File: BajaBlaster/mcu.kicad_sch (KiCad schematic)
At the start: 4 parts, among them U1 ESP32-WROOM-32

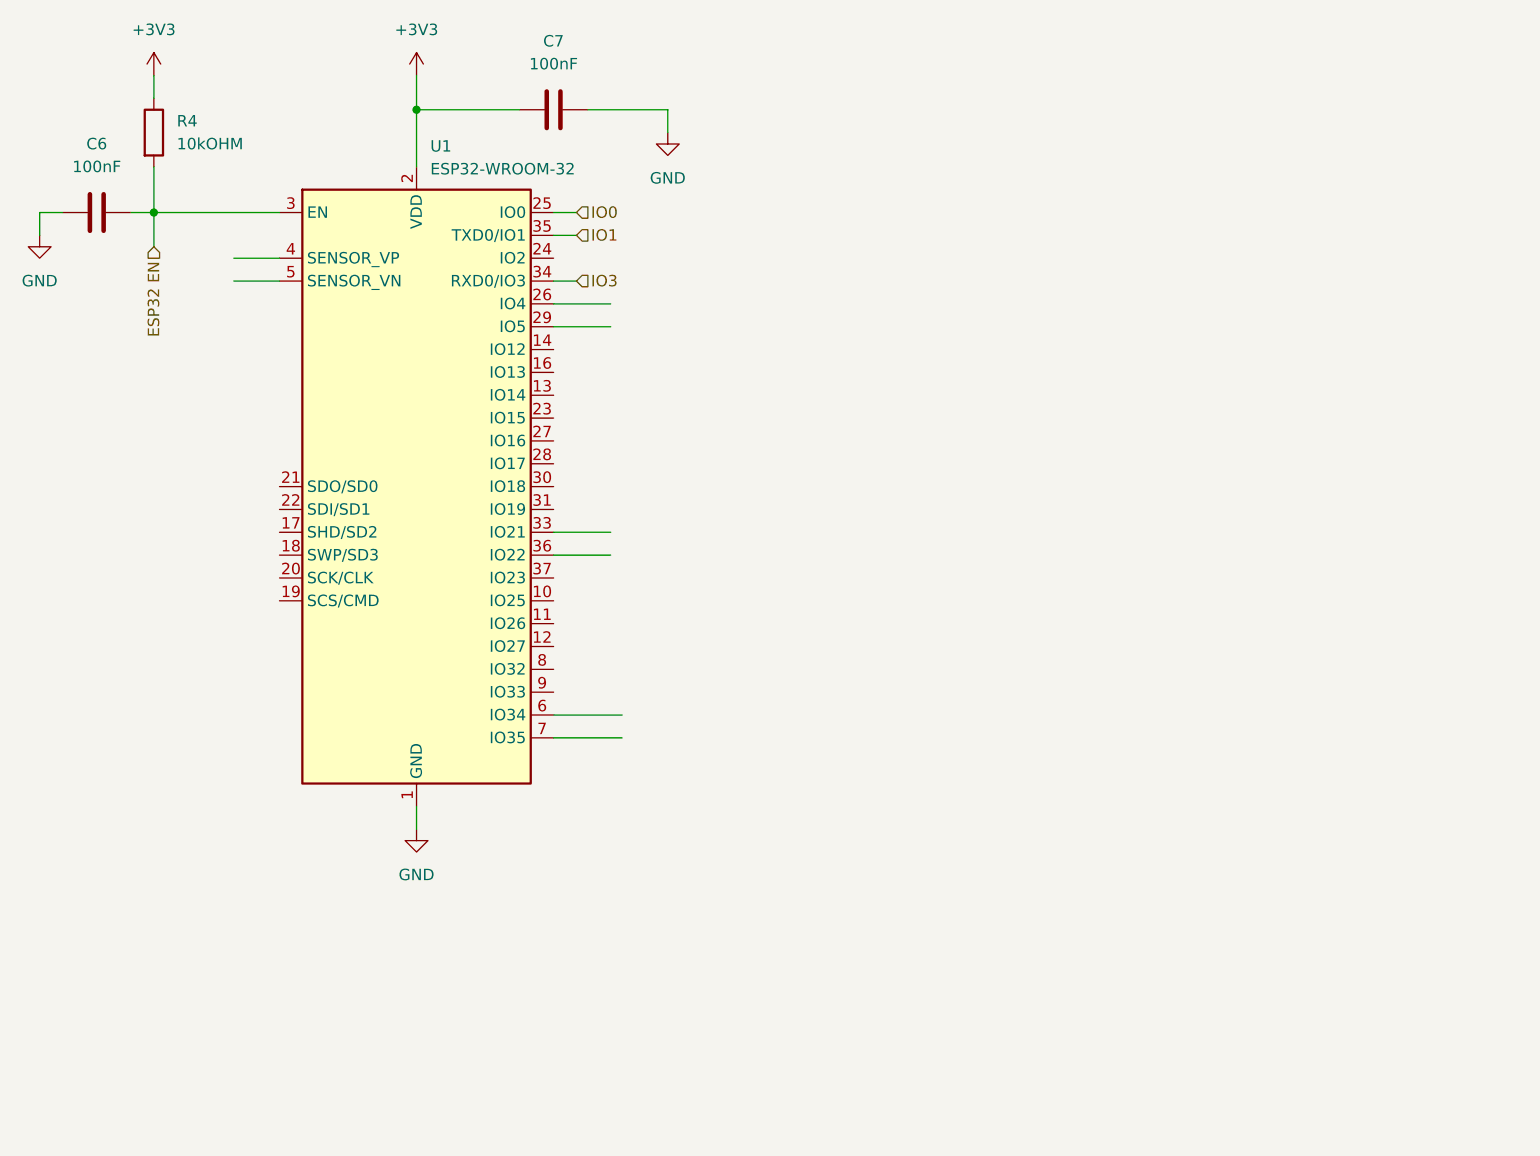
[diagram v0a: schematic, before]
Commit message: Updated mcu with wiring for MPU6050
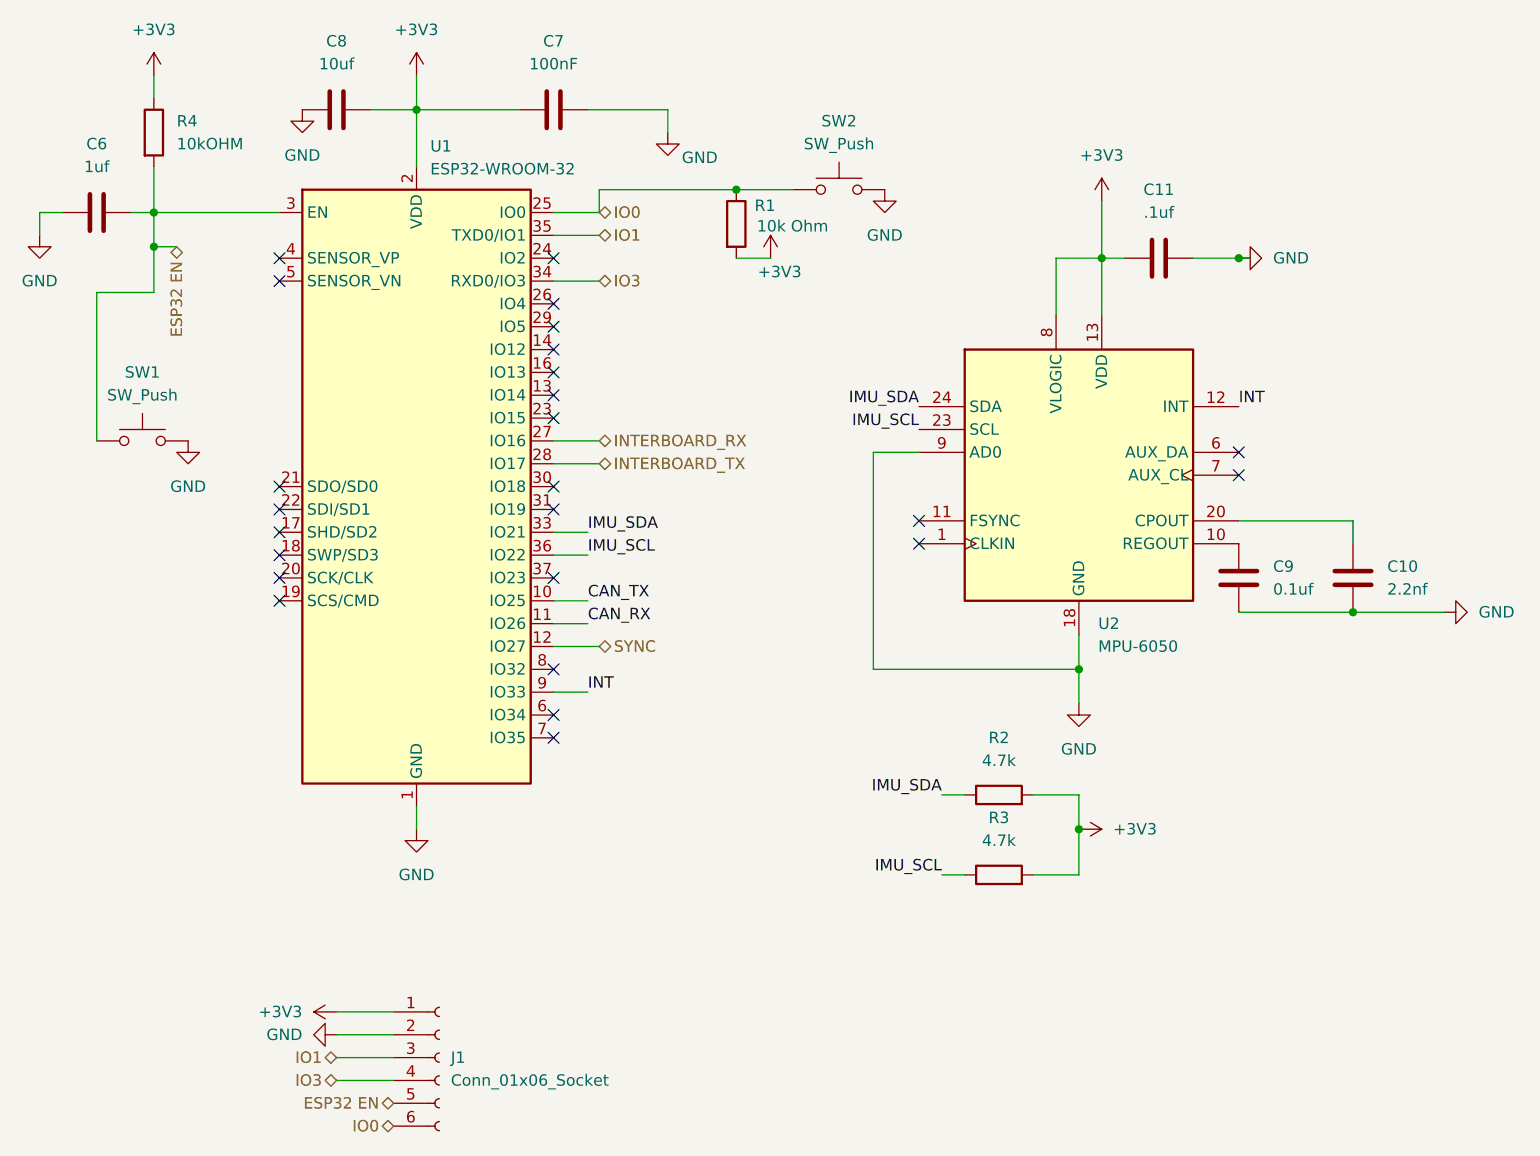
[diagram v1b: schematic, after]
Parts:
- added C10: 2.2nf, Package_SO:SOIC-8_3.9x4.9mm_P1.27mm, symbol Device:C
- added C11: .1uf, Package_SO:SOIC-8_3.9x4.9mm_P1.27mm, symbol Device:C
- added C8: 10uf, Package_SO:SOIC-8_3.9x4.9mm_P1.27mm, symbol Device:C
- added C9: 0.1uf, Package_SO:SOIC-8_3.9x4.9mm_P1.27mm, symbol Device:C
- added J1: Conn_01x06_Socket, Connector:Tag-Connect_TC2030-IDC-FP_2x03_P1.27mm_Vertical, symbol Connector:Conn_01x06_Socket
- added R1: 10k Ohm, Package_DIP:DIP-8_W7.62mm, symbol Device:R
- added R2, R3: 4.7k, Package_DIP:DIP-8_W7.62mm, symbol Device:R
- added SW1: SW_Push, Package_DIP:DIP-24_W7.62mm, symbol Switch:SW_Push
- added SW2: SW_Push, symbol Switch:SW_Push
- added U2: MPU-6050, Sensor_Motion:InvenSense_QFN-24_4x4mm_P0.5mm, symbol Sensor_Motion:MPU-6050
- C6: value 100nF -> 1uf
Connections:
- net +3V3: now also C11.1, C8.2, J1.1 (Pin_1), R1.2, R2.2, R3.2, U2.13 (VDD), U2.8 (VLOGIC)
- net ESP32 EN: now also J1.5 (Pin_5), SW1.1
- net GND: now also C10.1, C11.2, C8.1, C9.1, J1.2 (Pin_2), SW1.2, SW2.2, U2.18 (GND), U2.9 (AD0)
- net IO0: now also J1.6 (Pin_6), R1.1, SW2.1
- net IO1: now also J1.3 (Pin_3)
- net IO3: now also J1.4 (Pin_4)
- net CAN_TX: now reaches U1.10 (IO25)
- net CAN_RX: now reaches U1.11 (IO26)
- net SYNC: now reaches U1.12 (IO27)
- net INTERBOARD_RX: now reaches U1.27 (IO16)
- net INTERBOARD_TX: now reaches U1.28 (IO17)
- net IMU_SDA: now reaches U1.33 (IO21)
- net IMU_SDA: now also R2.1, U2.24 (SDA)
- net IMU_SCL: now reaches U1.36 (IO22)
- net IMU_SCL: now also R3.1, U2.23 (SCL)
- net INT: now reaches U1.9 (IO33)
- net INT: now also U2.12 (INT)
- new net: C9.2, U2.10 (REGOUT)
- new net: C10.2, U2.20 (CPOUT)
- no-connect marks 0 -> 25

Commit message: added new h tags
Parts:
- removed C10: 2.2nf, Package_SO:SOIC-8_3.9x4.9mm_P1.27mm, symbol Device:C
- removed C11: .1uf, Package_SO:SOIC-8_3.9x4.9mm_P1.27mm, symbol Device:C
- removed C8: 10uf, Package_SO:SOIC-8_3.9x4.9mm_P1.27mm, symbol Device:C
- removed C9: 0.1uf, Package_SO:SOIC-8_3.9x4.9mm_P1.27mm, symbol Device:C
- removed J1: Conn_01x06_Socket, Connector:Tag-Connect_TC2030-IDC-FP_2x03_P1.27mm_Vertical, symbol Connector:Conn_01x06_Socket
- removed R1: 10k Ohm, Package_DIP:DIP-8_W7.62mm, symbol Device:R
- removed R2, R3: 4.7k, Package_DIP:DIP-8_W7.62mm, symbol Device:R
- removed SW1: SW_Push, Package_DIP:DIP-24_W7.62mm, symbol Switch:SW_Push
- removed SW2: SW_Push, symbol Switch:SW_Push
- removed U2: MPU-6050, Sensor_Motion:InvenSense_QFN-24_4x4mm_P0.5mm, symbol Sensor_Motion:MPU-6050
- C6: value 1uf -> 100nF
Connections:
- net CAN_RX: no longer names the net of U1.11 (IO26)
- net CAN_TX: no longer names the net of U1.10 (IO25)
- net IMU_SCL: no longer names the net of U1.36 (IO22)
- net IMU_SDA: no longer names the net of U1.33 (IO21)
- net INT: no longer names the net of U1.9 (IO33)
- net INTERBOARD_RX: no longer names the net of U1.27 (IO16)
- net INTERBOARD_TX: no longer names the net of U1.28 (IO17)
- net SYNC: no longer names the net of U1.12 (IO27)
- no-connect marks 25 -> 0
